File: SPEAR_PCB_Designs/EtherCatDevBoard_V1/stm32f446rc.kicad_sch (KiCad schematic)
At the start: 32 parts, among them J1 USB_C_Receptacle_USB2.0_16P, J2 FTSH-107-01-F-DV-K-P-TR, J3 Conn_01x21_Pin, J4 Conn_01x21_Pin, SW1 SW_Push, U1 USBLC6-2SC6, U2 STM32F446RCT6, U3 AMS1117-3.3, Y1 16MHz

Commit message: Henry's continued work on the EtherCAT microcontroller dev. board.
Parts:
- D1: footprint LED_SMD:LED_0402_1005Metric -> LED_SMD:LED_0603_1608Metric
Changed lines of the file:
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@@
 			)
 		)
-		(property "Footprint" "LED_SMD:LED_0402_1005Metric"
+		(property "Footprint" "LED_SMD:LED_0603_1608Metric"
 			(at 156.21 172.72 0)
 			(effects

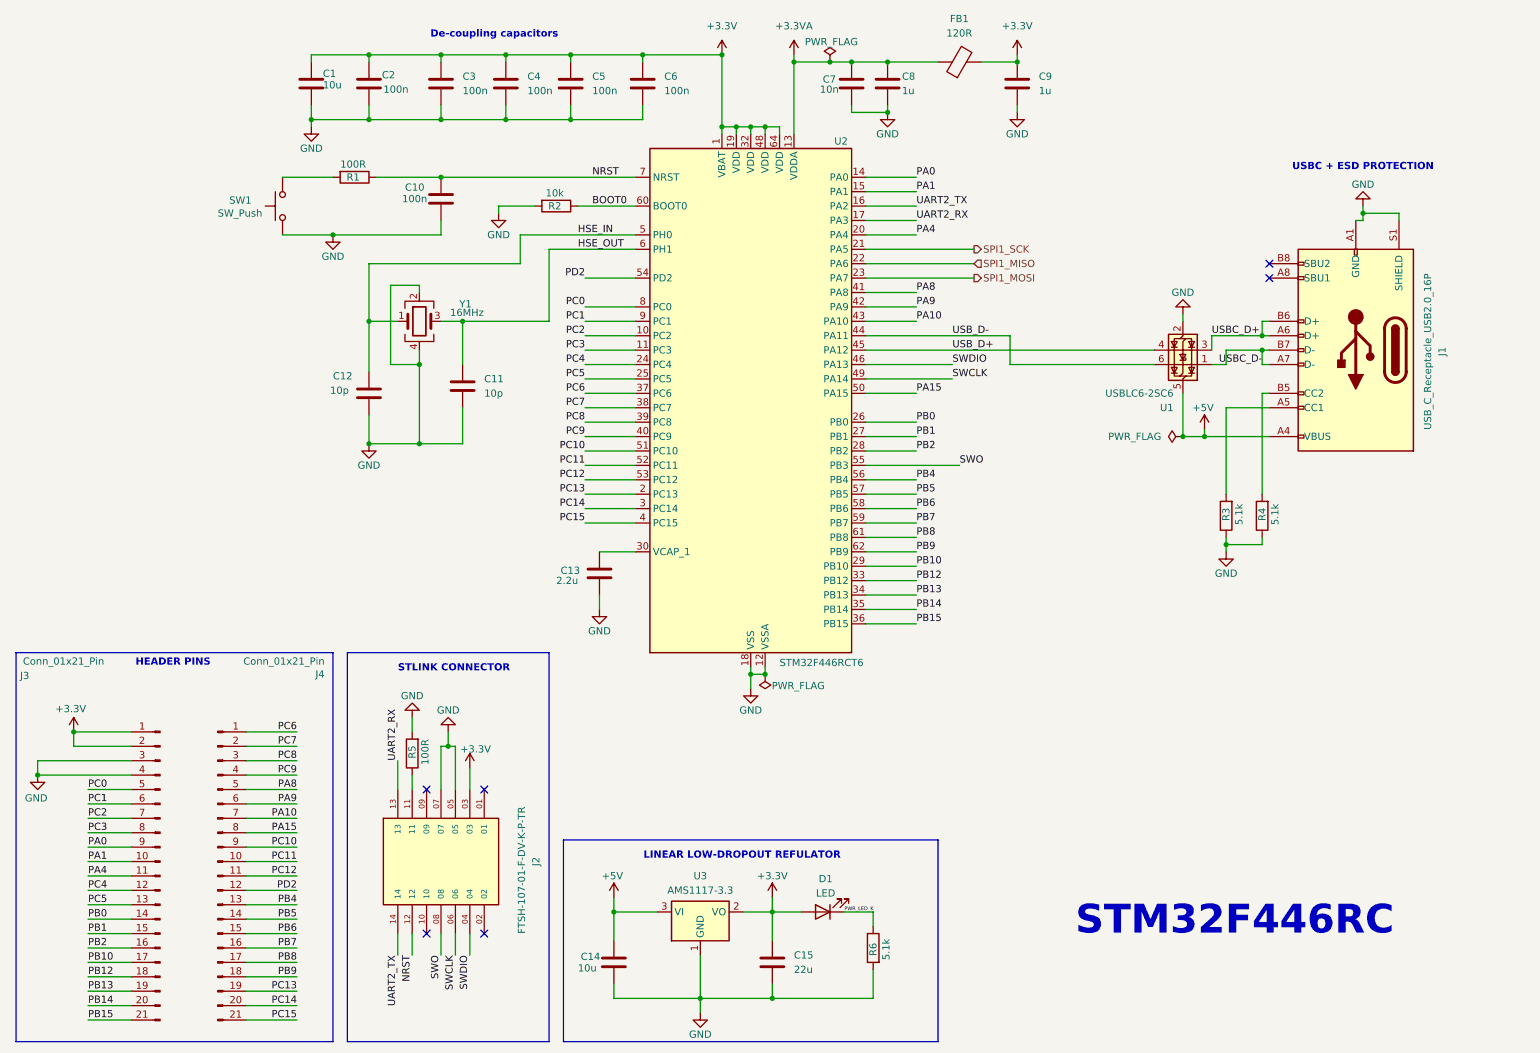
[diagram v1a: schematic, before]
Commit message: Continued work on the pcb layout of the EtherCAT uC dev board. Updated schematic to use a power mux.
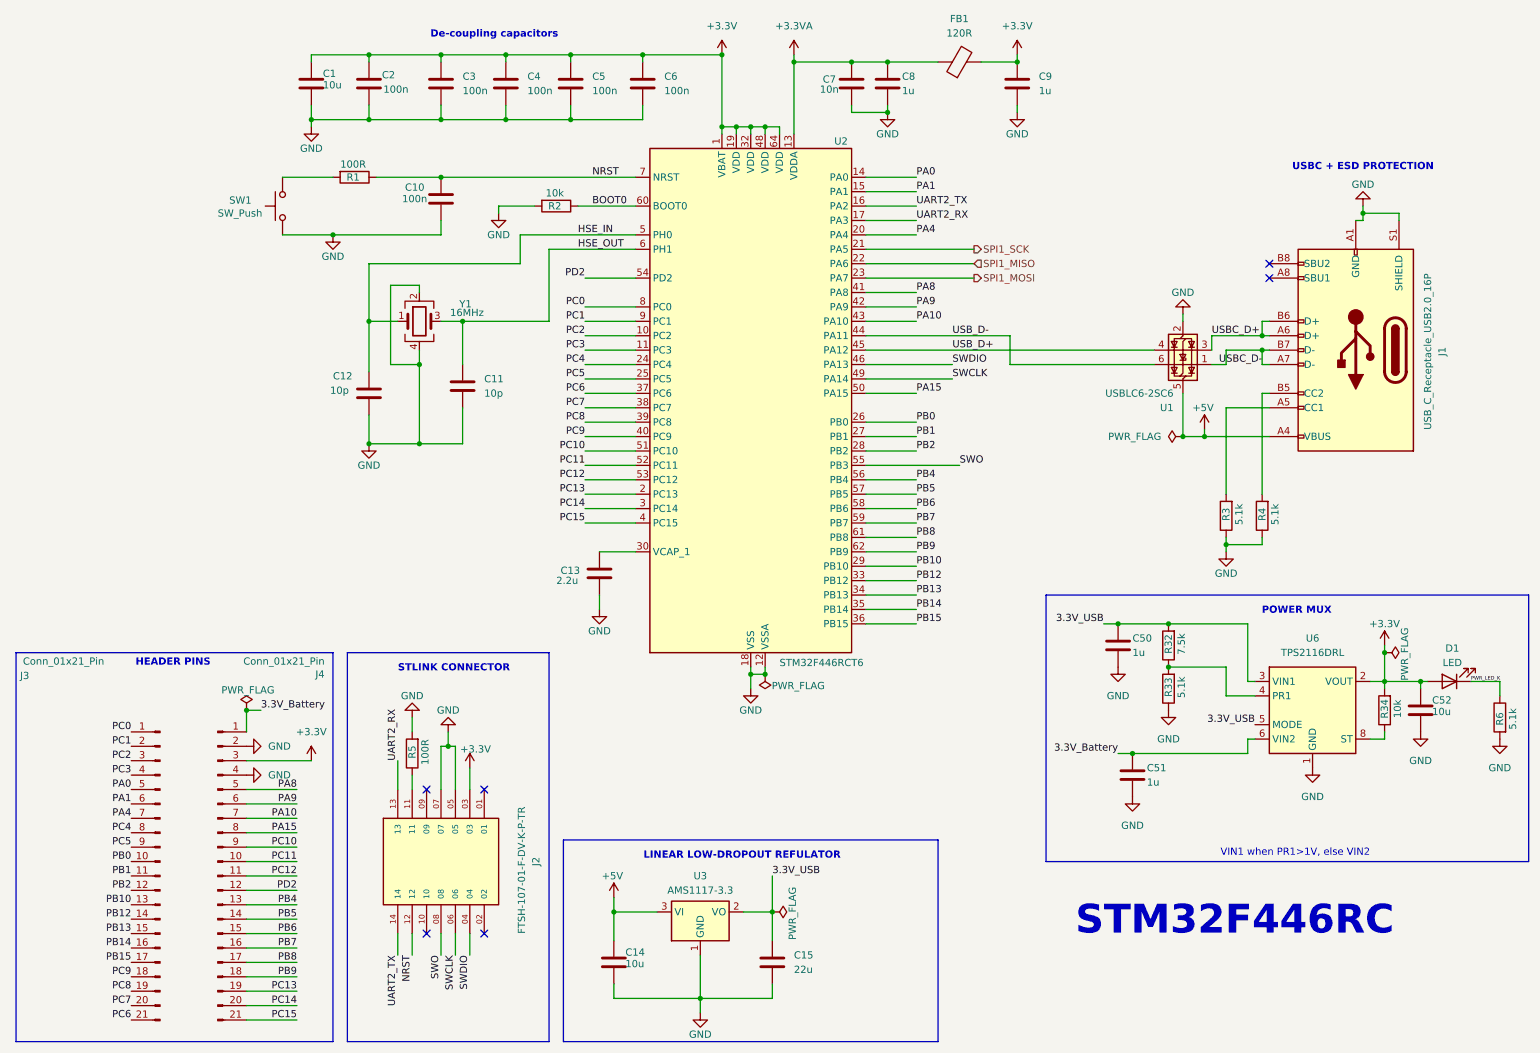
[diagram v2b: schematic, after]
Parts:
- added C50, C51: 1u, Capacitor_SMD:C_0402_1005Metric, symbol Device:C
- added C52: 10u, Capacitor_SMD:C_0603_1608Metric, symbol Device:C
- added R32: 7.5k, Resistor_SMD:R_0402_1005Metric, symbol Device:R
- added R33: 5.1k, Resistor_SMD:R_0402_1005Metric, symbol Device:R
- added R34: 10k, Resistor_SMD:R_0402_1005Metric, symbol Device:R
- added U6: TPS2116DRL, Package_TO_SOT_SMD:SOT-583-8, symbol Power_Management:TPS2116DRL
- C14: footprint Capacitor_SMD:C_0402_1005Metric -> Capacitor_SMD:C_0603_1608Metric
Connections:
- net +3.3V: now also J4.3 (Pin_3), C52.1, R34.2, U6.2 (VOUT), U6.7 (VOUT); no longer C15.1, J3.1 (Pin_1), J3.2 (Pin_2), U3.2 (VO)
- net GND: now also J4.2 (Pin_2), J4.4 (Pin_4), C50.2, C51.2, C52.2, R33.1, U6.1 (GND); no longer J3.3 (Pin_3), J3.4 (Pin_4)
- net PA0: now also J3.5 (Pin_5); no longer J3.9 (Pin_9)
- net PA1: now also J3.6 (Pin_6); no longer J3.10 (Pin_10)
- net PA4: now also J3.7 (Pin_7); no longer J3.11 (Pin_11)
- net PB0: now also J3.10 (Pin_10); no longer J3.14 (Pin_14)
- net PB1: now also J3.11 (Pin_11); no longer J3.15 (Pin_15)
- net PB10: now also J3.13 (Pin_13); no longer J3.17 (Pin_17)
- net PB12: now also J3.14 (Pin_14); no longer J3.18 (Pin_18)
- net PB13: now also J3.15 (Pin_15); no longer J3.19 (Pin_19)
- net PB14: now also J3.16 (Pin_16); no longer J3.20 (Pin_20)
- net PB15: now also J3.17 (Pin_17); no longer J3.21 (Pin_21)
- net PB2: now also J3.12 (Pin_12); no longer J3.16 (Pin_16)
- net PC0: now also J3.1 (Pin_1); no longer J3.5 (Pin_5)
- net PC1: now also J3.2 (Pin_2); no longer J3.6 (Pin_6)
- net PC2: now also J3.3 (Pin_3); no longer J3.7 (Pin_7)
- net PC3: now also J3.4 (Pin_4); no longer J3.8 (Pin_8)
- net PC4: now also J3.8 (Pin_8); no longer J3.12 (Pin_12)
- net PC5: now also J3.9 (Pin_9); no longer J3.13 (Pin_13)
- net PC6: now also J3.21 (Pin_21); no longer J4.1 (Pin_1)
- net PC7: now also J3.20 (Pin_20); no longer J4.2 (Pin_2)
- net PC8: now also J3.19 (Pin_19); no longer J4.3 (Pin_3)
- net PC9: now also J3.18 (Pin_18); no longer J4.4 (Pin_4)
- new net: R34.1, U6.8 (ST)
- new net: R32.1, R33.2, U6.4 (PR1)
- new net 3.3V_Battery: C51.1, J4.1 (Pin_1), U6.6 (VIN2)
- new net 3.3V_USB: C15.1, C50.1, R32.2, U3.2 (VO), U6.3 (VIN1), U6.5 (MODE)
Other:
- note added: "POWER MUX"
- note added: "VIN1 when PR1>1V, else VIN2"
- moved on the sheet: D1, R6

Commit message: Edited schematic to fix problems with Lan9252. Continued work on pcb layout.
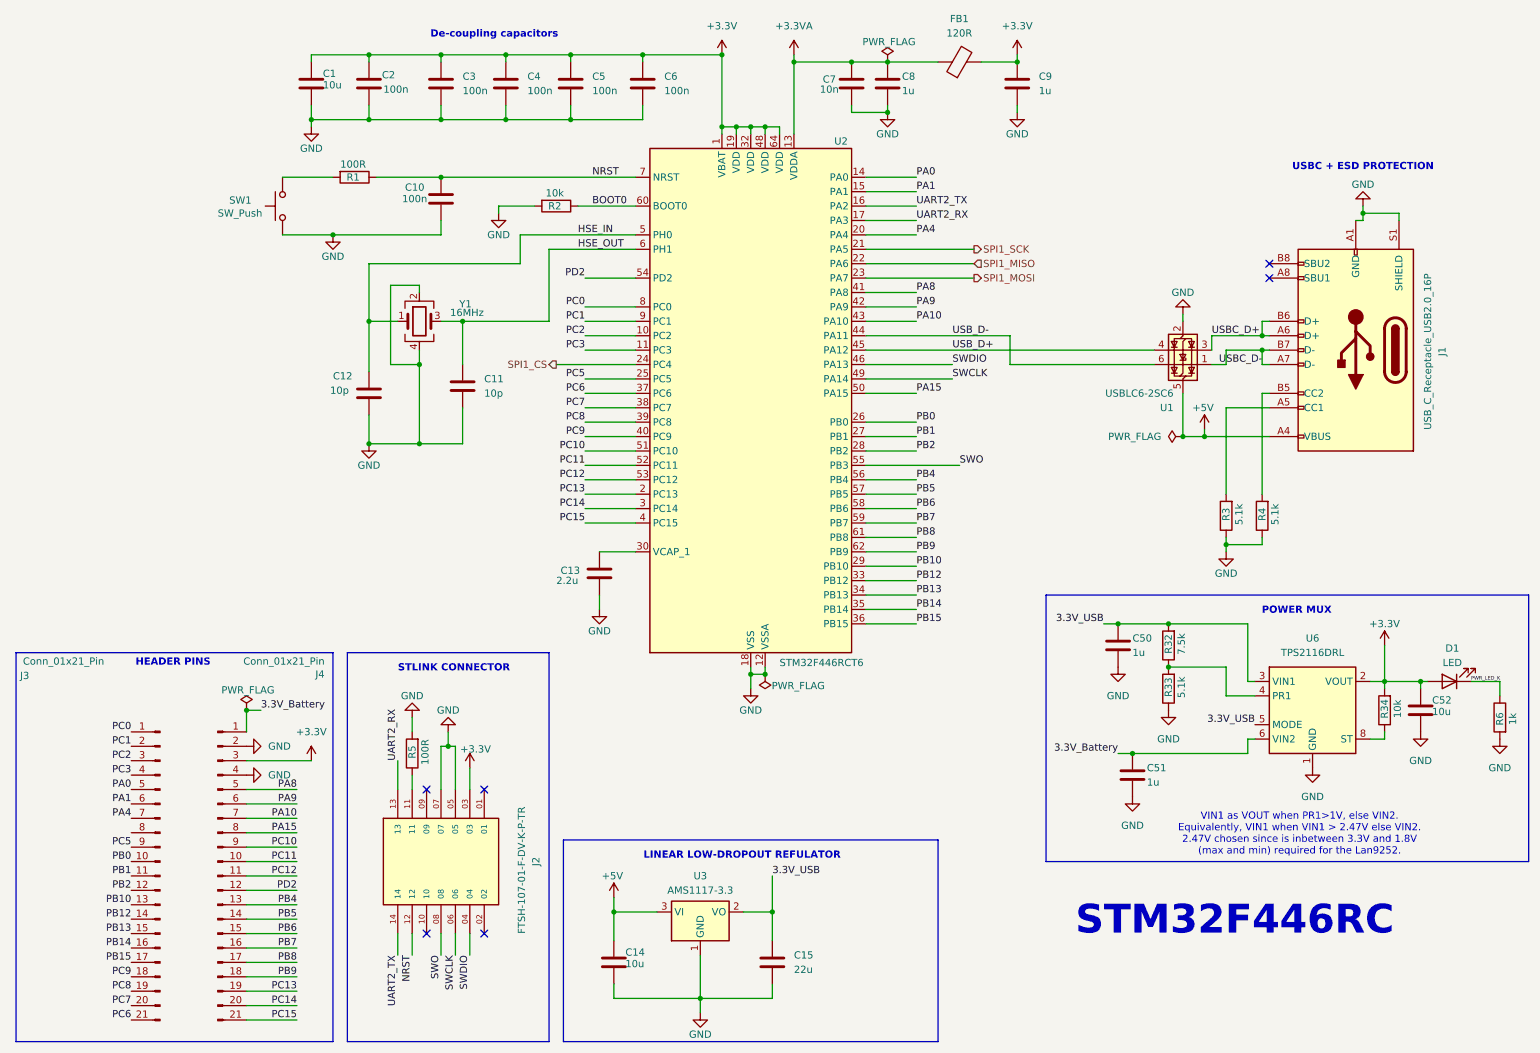
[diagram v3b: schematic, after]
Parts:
- R6: value 5.1k -> 1k
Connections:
- net PC4: no longer names the net of J3.8 (Pin_8)
- net PC4: no longer U2.24 (PC4)
- new net SPI1_CS: U2.24 (PC4)
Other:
- note added: "VIN1 as VOUT when PR1>1V, else VIN2. Equivalently, VIN1 when VIN1 > 2.47V else VIN2. 2.47V chosen since is inbetween 3.3V and 1.8V (max and min) required for the Lan9252."
- note removed: "VIN1 when PR1>1V, else VIN2"
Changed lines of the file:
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@@
 		)
 	)
-	(text "VIN1 when PR1>1V, else VIN2"
+	(text "VIN1 as VOUT when PR1>1V, else VIN2.\nEquivalently, VIN1 when VIN1 > 2.47V else VIN2.\n2.47V chosen since is inbetween 3.3V and 1.8V\n(max and min) required for the Lan9252."
 		(exclude_from_sim no)
-		(at 239.522 162.306 0)
+		(at 240.284 159.004 0)
 		(effects
 			(font
@@
 	)
 	(junction
-		(at 255.27 127)
-		(diameter 0)
-		(color 0 0 0 0)
-	)
-	(junction
 		(at 208.28 121.92)
 		(diameter 0)
@@
 	(wire
 		(pts
-			(xy 255.27 127) (xy 255.27 132.08)
-		)
-		(stroke
-			(width 0)
-			(type default)
-		)
-	)
-	(wire
-		(pts
 			(xy 190.5 21.59) (xy 190.5 22.86)
 		)
@@
 	(wire
 		(pts
-			(xy 114.3 76.2) (xy 123.19 76.2)
+			(xy 109.22 76.2) (xy 123.19 76.2)
 		)
 		(stroke
@@
 	(wire
 		(pts
-			(xy 255.27 125.73) (xy 255.27 127)
+			(xy 255.27 125.73) (xy 255.27 132.08)
 		)
 		(stroke
@@
 		)
 	)
-	(label "PC4"
-		(at 114.3 76.2 180)
-		(effects
-			(font
-				(size 1.27 1.27)
-			)
-			(justify right bottom)
-		)
-	)
 	(label "PB0"
 		(at 172.72 86.36 0)
@@
 		)
 	)
-	(label "PC4"
-		(at 34.29 158.75 180)
-		(effects
-			(font
-				(size 1.27 1.27)
-			)
-			(justify right bottom)
-		)
-	)
 	(label "USBC_D-"
 		(at 226.06 76.2 0)
@@
 		)
 	)
+	(hierarchical_label "SPI1_CS"
+		(shape output)
+		(at 109.22 76.2 180)
+		(effects
+			(font
+				(size 1.27 1.27)
+			)
+			(justify right)
+		)
+	)
 	(symbol
 		(lib_id "Device:C")
@@
 	)
 	(symbol
-		(lib_id "power:PWR_FLAG")
-		(at 147.32 172.72 270)
-		(unit 1)
-		(exclude_from_sim no)
-		(in_bom yes)
-		(on_board yes)
-		(dnp no)
-		(property "Reference" "#FLG010"
-			(at 149.225 172.72 0)
-			(effects
-				(font
-					(size 1.27 1.27)
-				)
-				(hide yes)
-			)
-		)
-		(property "Value" "PWR_FLAG"
-			(at 150.876 172.974 0)
-			(effects
-				(font
-					(size 1.27 1.27)
-				)
-			)
-		)
-		(property "Footprint" ""
-			(at 147.32 172.72 0)
-			(effects
-				(font
-					(size 1.27 1.27)
-				)
-				(hide yes)
-			)
-		)
-		(property "Datasheet" "~"
-			(at 147.32 172.72 0)
-			(effects
-				(font
-					(size 1.27 1.27)
-				)
-				(hide yes)
-			)
-		)
-		(property "Description" "Special symbol for telling ERC where power comes from"
-			(at 147.32 172.72 0)
-			(effects
-				(font
-					(size 1.27 1.27)
-				)
-				(hide yes)
-			)
-		)
-		(pin "1"
-		)
-		(instances
-			(project "SPEAR_V1"
-				(path "/6af343d7-7346-4b6a-90ee-eb113982f4e5/ad078953-06c7-4dc0-a658-e8fb86486200"
-					(reference "#FLG010")
-					(unit 1)
-				)
-			)
-		)
-	)
-	(symbol
 		(lib_id "power:GND")
 		(at 143.51 133.35 0)
@@
 			)
 		)
-		(property "Value" "5.1k"
+		(property "Value" "1k"
 			(at 277.876 138.684 90)
 			(effects
@@
 	)
 	(symbol
-		(lib_id "power:PWR_FLAG")
-		(at 255.27 127 270)
-		(unit 1)
-		(exclude_from_sim no)
-		(in_bom yes)
-		(on_board yes)
-		(dnp no)
-		(property "Reference" "#FLG01"
-			(at 257.175 127 0)
-			(effects
-				(font
-					(size 1.27 1.27)
-				)
-				(hide yes)
-			)
-		)
-		(property "Value" "PWR_FLAG"
-			(at 258.826 127.254 0)
-			(effects
-				(font
-					(size 1.27 1.27)
-				)
-			)
-		)
-		(property "Footprint" ""
-			(at 255.27 127 0)
-			(effects
-				(font
-					(size 1.27 1.27)
-				)
-				(hide yes)
-			)
-		)
-		(property "Datasheet" "~"
-			(at 255.27 127 0)
-			(effects
-				(font
-					(size 1.27 1.27)
-				)
-				(hide yes)
-			)
-		)
-		(property "Description" "Special symbol for telling ERC where power comes from"
-			(at 255.27 127 0)
-			(effects
-				(font
-					(size 1.27 1.27)
-				)
-				(hide yes)
-			)
-		)
-		(pin "1"
-		)
-		(instances
-			(project "SPEAR_V1"
-				(path "/6af343d7-7346-4b6a-90ee-eb113982f4e5/ad078953-06c7-4dc0-a658-e8fb86486200"
-					(reference "#FLG01")
-					(unit 1)
-				)
-			)
-		)
-	)
-	(symbol
 		(lib_id "power:GND")
 		(at 217.17 137.16 0)
@@
 					(unit 1)
 				)
+			)
+		)
+	)
+	(symbol
+		(lib_id "power:PWR_FLAG")
+		(at 167.64 22.86 0)
+		(unit 1)
+		(exclude_from_sim no)
+		(in_bom yes)
+		(on_board yes)
+		(dnp no)
+		(property "Reference" "#FLG01"
+			(at 167.64 20.955 0)
+			(effects
+				(font
+					(size 1.27 1.27)
+				)
+				(hide yes)
+			)
+		)
+		(property "Value" "PWR_FLAG"
+			(at 167.894 19.304 0)
+			(effects
+				(font
+					(size 1.27 1.27)
+				)
+			)
+		)
+		(property "Footprint" ""
+			(at 167.64 22.86 0)
+			(effects
+				(font
+					(size 1.27 1.27)
+				)
+				(hide yes)
+			)
+		)
+		(property "Datasheet" "~"
+			(at 167.64 22.86 0)
+			(effects
+				(font
+					(size 1.27 1.27)
+				)
+				(hide yes)
+			)
+		)
+		(property "Description" "Special symbol for telling ERC where power comes from"
+			(at 167.64 22.86 0)
+			(effects
+				(font
+					(size 1.27 1.27)
+				)
+				(hide yes)
+			)
+		)
+		(pin "1"
+		)
+		(instances
+			(project "SPEAR_V1"
+				(path "/6af343d7-7346-4b6a-90ee-eb113982f4e5/ad078953-06c7-4dc0-a658-e8fb86486200"
+					(reference "#FLG01")
+					(unit 1)
+				)
